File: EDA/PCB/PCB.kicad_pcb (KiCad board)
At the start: 2 copper layers, 73.8 x 48.9 mm, 12 parts, among them J1 Conn_01x06_Female, J2 Screw_Terminal_01x02, J3 Screw_Terminal_01x03, U1 PC817, U2 PC817, U3 WeMos_D1_mini, U4 PC817

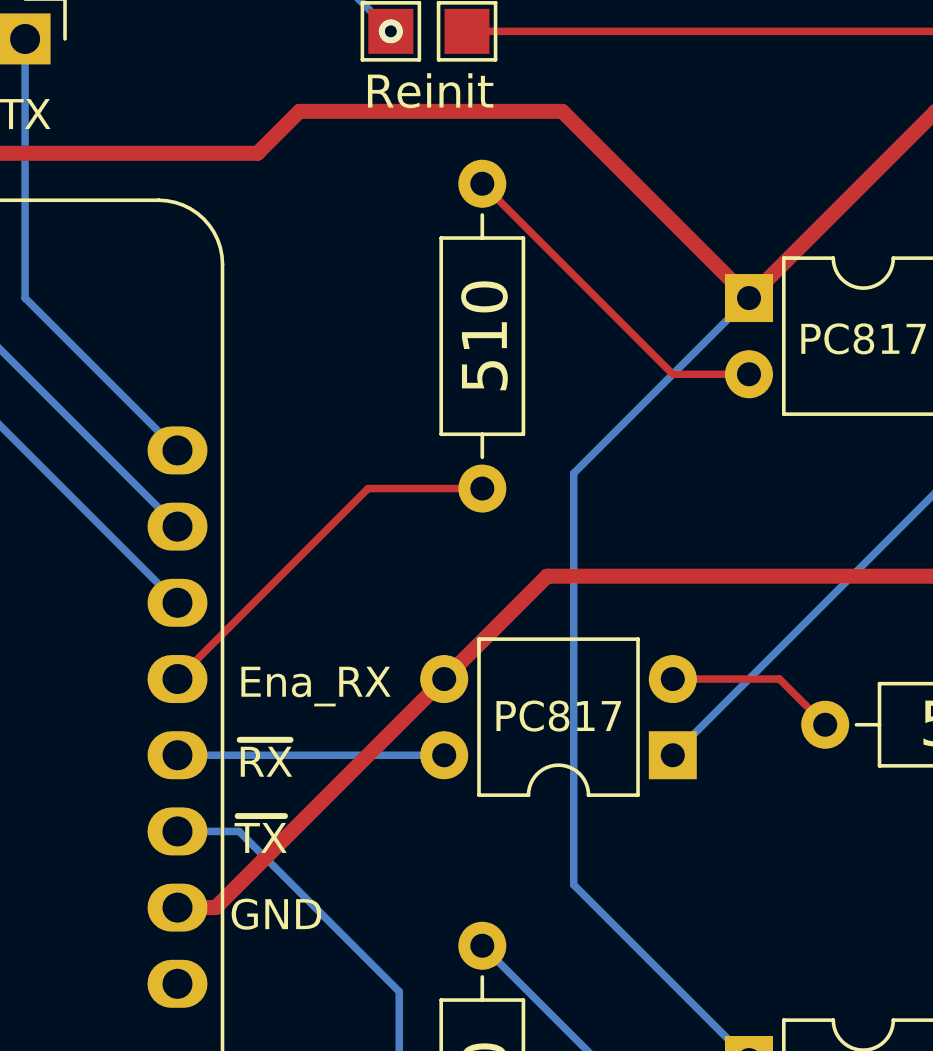
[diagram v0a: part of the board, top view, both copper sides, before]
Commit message: Update PCB's legends
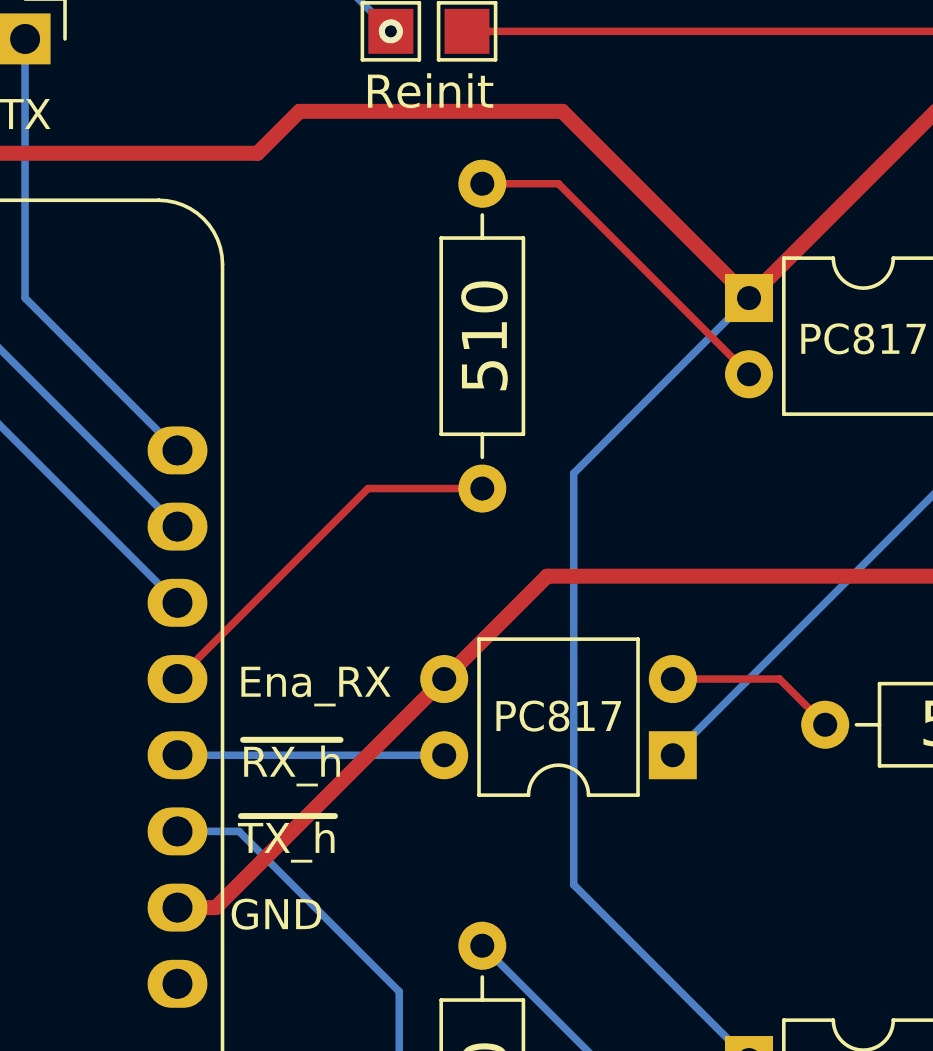
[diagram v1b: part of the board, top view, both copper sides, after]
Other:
- board text added: "~RX_h"
- board text added: "~TX_h"
- board text removed: "~RX"
- board text removed: "~TX"

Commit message: Update PCB.kicad_pcb
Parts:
- added J4: Conn_01x02_Male, Connector_PinHeader_2.54mm:PinHeader_1x02_P2.54mm_Vertical, F.Cu at (104.9, 92.5)
- added J5: Conn_01x03_Male, Connector_PinHeader_2.54mm:PinHeader_1x03_P2.54mm_Vertical, F.Cu at (104.9, 113.0)
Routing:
- net Net-(J3-Pad3): track 20.5 -> 29.7 mm
- net Net-(J2-Pad2): track 131.5 -> 138.9 mm
- net Net-(J3-Pad1): track 13.8 -> 17.1 mm
- net Net-(J2-Pad1): track 91.1 -> 93.0 mm
- net Net-(J3-Pad2): track 24.9 -> 25.5 mm
